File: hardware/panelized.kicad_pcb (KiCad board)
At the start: 2 copper layers, 69.2 x 21 mm, 90 parts, among them J1 USB_B_Micro, J12 Conn_01x01, J2 Conn_01x01, J3 Conn_01x01, J4 Conn_01x01, Q1 Q_DUAL_NPN_NPN_E1B1C2E2B2C1, Q2 Q_PMOS_GSD, Q3 Q_PMOS_GSD, U1 MCP73831-2-OT, U2 CP2104, U3 TPS62400, U4 ESP32-PICO-D4, U5 BD48KxxG

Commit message: To be continued
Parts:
- removed the C1 at (114.8, 106.5)
- removed the C1 at (114.8, 118.5)
- removed C10 (x2), C11 (x2), C13 (x2): 10μF, Capacitor_SMD:C_0402_1005Metric
- removed C12 (x2): 33pF, Capacitor_SMD:C_0402_1005Metric
- removed the C2 at (111.8, 101.1)
- removed the C2 at (111.8, 113.1)
- removed the C5 at (139.0, 103.8)
- removed the C5 at (139.0, 115.8)
- removed the C7 at (138.3, 106.9)
- removed the C7 at (138.3, 118.9)
- removed the D1 at (113.7, 107.7)
- removed the D1 at (113.7, 119.7)
- removed the D2 at (101.1, 102.4)
- removed the D2 at (101.1, 114.4)
- removed the D3 at (112.1, 105.8)
- removed the D3 at (112.1, 117.8)
- removed the JP1 at (137.5, 100.8)
- removed the JP1 at (137.5, 112.8)
- removed L2 (x2), L3 (x2): 2.2μH, Inductor_SMD:L_0805_2012Metric
- removed the Q1 at (137.1, 102.9)
- removed the Q1 at (137.1, 114.9)
- removed the Q3 at (111.8, 103.8)
- removed the Q3 at (111.8, 115.8)
- removed the R10 at (109.0, 101.4)
- removed the R10 at (109.0, 113.4)
- removed the R11 at (108.0, 107.5)
- removed the R11 at (108.0, 119.5)
- removed the R12 at (110.0, 107.5)
- removed the R12 at (110.0, 119.5)
- removed the R14 at (111.7, 106.8)
- removed the R14 at (111.7, 118.8)
- removed the R2 at (114.8, 105.0)
- removed the R2 at (114.8, 117.0)
- removed the R3 at (117.7, 105.9)
- removed the R3 at (117.7, 117.9)
- removed the R4 at (115.7, 107.7)
- removed the R4 at (115.7, 119.7)
- removed R5 (x2): 470kΩ, Resistor_SMD:R_0402_1005Metric
- removed the R6 at (109.2, 105.6)
- removed the R6 at (109.2, 117.6)
- removed the R7 at (126.8, 102.0)
- removed the R7 at (126.8, 114.0)
- removed the R8 at (125.6, 102.0)
- removed the R8 at (125.6, 114.0)
- removed the R9 at (108.0, 101.4)
- removed the R9 at (108.0, 113.4)
- removed the REF** at (98.3, 116.5)
- removed the REF** at (98.3, 104.5)
- removed the U1 at (114.8, 102.0)
- removed the U1 at (114.8, 114.0)
- removed the U3 at (105.7, 104.4)
- removed the U3 at (105.7, 116.4)
- removed the U4 at (131.5, 104.2)
- removed the U4 at (131.5, 116.2)
- removed the U5 at (103.7, 101.7)
- removed the U5 at (103.7, 113.7)
- added C1: 4.7μF, Capacitor_SMD:C_0402_1005Metric, F.Cu at (116.0, 118.1)
- added C1: 4.7μF, Capacitor_SMD:C_0402_1005Metric, F.Cu at (116.0, 106.1)
- added C2: 4.7μF, Capacitor_SMD:C_0402_1005Metric, F.Cu at (111.6, 113.1)
- added C2: 4.7μF, Capacitor_SMD:C_0402_1005Metric, F.Cu at (111.6, 101.1)
- added C3: 4.7μF, Capacitor_SMD:C_0402_1005Metric, F.Cu at (139.0, 115.8)
- added C3: 4.7μF, Capacitor_SMD:C_0402_1005Metric, F.Cu at (139.0, 103.8)
- added C4: 4.7μF, Capacitor_SMD:C_0402_1005Metric, F.Cu at (108.9, 115.6)
- added C4: 4.7μF, Capacitor_SMD:C_0402_1005Metric, F.Cu at (108.9, 103.6)
- added C5: 10μF, Capacitor_SMD:C_0402_1005Metric, F.Cu at (103.1, 114.9)
- added C5: 10μF, Capacitor_SMD:C_0402_1005Metric, F.Cu at (103.1, 102.9)
- added C6: 120pF, Capacitor_SMD:C_0402_1005Metric, F.Cu at (105.0, 119.3)
- added C6: 120pF, Capacitor_SMD:C_0402_1005Metric, F.Cu at (105.0, 107.3)
- added C7: 4.7μF, Capacitor_SMD:C_0402_1005Metric, F.Cu at (108.9, 116.6)
- added C7: 4.7μF, Capacitor_SMD:C_0402_1005Metric, F.Cu at (108.9, 104.6)
- added C8: 1.5pF, Capacitor_SMD:C_0402_1005Metric, F.Cu at (138.3, 118.9)
- added C8: 1.5pF, Capacitor_SMD:C_0402_1005Metric, F.Cu at (138.3, 106.9)
- added C9: 10μF, Capacitor_SMD:C_0402_1005Metric, F.Cu at (101.5, 115.6)
- added C9: 10μF, Capacitor_SMD:C_0402_1005Metric, F.Cu at (101.5, 103.6)
- added D1: LED_Small_ALT, LED_SMD:LED_0402_1005Metric, F.Cu at (114.5, 116.4)
- added D1: LED_Small_ALT, LED_SMD:LED_0402_1005Metric, F.Cu at (114.5, 104.4)
- added D2: D_ALT, Diode_SMD:D_0402_1005Metric, F.Cu at (101.5, 114.4)
- added D2: D_ALT, Diode_SMD:D_0402_1005Metric, F.Cu at (101.5, 102.4)
- added D3: D_Schottky, Diode_SMD:D_0402_1005Metric, F.Cu at (111.7, 117.5)
- added D3: D_Schottky, Diode_SMD:D_0402_1005Metric, F.Cu at (111.7, 105.5)
- added G***: LOGO, double-oh:OSHW_mark, B.Cu at (112.8, 115.3)
- added G***: LOGO, double-oh:OSHW_mark, B.Cu at (112.8, 103.3)
- added JP1: Jumper_NO_Small, double-oh:solder_bridge, F.Cu at (137.1, 113.2)
- added JP1: Jumper_NO_Small, double-oh:solder_bridge, F.Cu at (137.1, 101.2)
- added JP3: Jumper_NO_Small, double-oh:solder_bridge, F.Cu at (129.7, 119.5)
- added JP3: Jumper_NO_Small, double-oh:solder_bridge, F.Cu at (129.7, 107.5)
- added Q1: Q_DUAL_NPN_NPN_E1B1C2E2B2C1, Package_TO_SOT_SMD:SOT-363_SC-70-6, F.Cu at (137.1, 115.3)
- added Q1: Q_DUAL_NPN_NPN_E1B1C2E2B2C1, Package_TO_SOT_SMD:SOT-363_SC-70-6, F.Cu at (137.1, 103.3)
- added Q3: Q_PMOS_GSD, Package_TO_SOT_SMD:SOT-323_SC-70, F.Cu at (111.3, 115.3)
- added Q3: Q_PMOS_GSD, Package_TO_SOT_SMD:SOT-323_SC-70, F.Cu at (111.3, 103.3)
- added R10: 68kΩ, Resistor_SMD:R_0402_1005Metric, F.Cu at (104.8, 117.4)
- added R10: 68kΩ, Resistor_SMD:R_0402_1005Metric, F.Cu at (104.8, 105.4)
- added R11: 68kΩ, Resistor_SMD:R_0402_1005Metric, F.Cu at (109.2, 119.5)
- added R11: 68kΩ, Resistor_SMD:R_0402_1005Metric, F.Cu at (109.2, 107.5)
- added R12: 300kΩ, Resistor_SMD:R_0402_1005Metric, F.Cu at (110.2, 119.5)
- added R12: 300kΩ, Resistor_SMD:R_0402_1005Metric, F.Cu at (110.2, 107.5)
- added R14: 68kΩ, Resistor_SMD:R_0402_1005Metric, F.Cu at (111.7, 118.5)
- added R14: 68kΩ, Resistor_SMD:R_0402_1005Metric, F.Cu at (111.7, 106.5)
- added R2: 3kΩ, Resistor_SMD:R_0402_1005Metric, F.Cu at (117.1, 113.8)
- added R2: 3kΩ, Resistor_SMD:R_0402_1005Metric, F.Cu at (117.1, 101.8)
- added R3: 68kΩ, Resistor_SMD:R_0402_1005Metric, F.Cu at (117.7, 118.5)
- added R3: 68kΩ, Resistor_SMD:R_0402_1005Metric, F.Cu at (117.7, 106.5)
- added R4: 2kΩ, Resistor_SMD:R_0402_1005Metric, F.Cu at (116.5, 116.4)
- added R4: 2kΩ, Resistor_SMD:R_0402_1005Metric, F.Cu at (116.5, 104.4)
- added R6: 68kΩ, Resistor_SMD:R_0402_1005Metric, F.Cu at (104.4, 113.6)
- added R6: 68kΩ, Resistor_SMD:R_0402_1005Metric, F.Cu at (104.4, 101.6)
- added R7: 68kΩ, Resistor_SMD:R_0402_1005Metric, F.Cu at (126.2, 114.2)
- added R7: 68kΩ, Resistor_SMD:R_0402_1005Metric, F.Cu at (126.2, 102.2)
- added R8: 1kΩ, Resistor_SMD:R_0402_1005Metric, F.Cu at (126.2, 116.2)
- added R8: 1kΩ, Resistor_SMD:R_0402_1005Metric, F.Cu at (126.2, 104.2)
- added R9: 330kΩ, Resistor_SMD:R_0402_1005Metric, F.Cu at (103.9, 119.3)
- added R9: 330kΩ, Resistor_SMD:R_0402_1005Metric, F.Cu at (103.9, 107.3)
- added REF**: mousebite_mount, double-oh:mousebite_mount, F.Cu at (98.4, 104.5)
- added REF**: mousebite_mount, double-oh:mousebite_mount, F.Cu at (98.4, 116.5)
- added REF**: Fiducial_0.5mm_Mask1.5mm, Fiducial:Fiducial_0.5mm_Mask1.5mm, F.Cu at (146.5, 115.6)
- added REF**: Fiducial_0.5mm_Mask1.5mm, Fiducial:Fiducial_0.5mm_Mask1.5mm, F.Cu at (99.5, 117.3)
- added REF**: Fiducial_0.5mm_Mask1.5mm, Fiducial:Fiducial_0.5mm_Mask1.5mm, F.Cu at (99.5, 105.3)
- added REF**: Fiducial_0.5mm_Mask1.5mm, Fiducial:Fiducial_0.5mm_Mask1.5mm, F.Cu at (146.5, 103.6)
- added U1: MCP73831-2-OT, Package_TO_SOT_SMD:SOT-23-5, F.Cu at (114.7, 114.0)
- added U1: MCP73831-2-OT, Package_TO_SOT_SMD:SOT-23-5, F.Cu at (114.7, 102.0)
- added U3: TPSM828x, double-oh:microSiL-10, F.Cu at (105.2, 115.5)
- added U3: TPSM828x, double-oh:microSiL-10, F.Cu at (105.2, 103.5)
- added U4: ESP32-U4WDH, Package_DFN_QFN:QFN-48-1EP_5x5mm_P0.35mm_EP3.7x3.7mm, F.Cu at (131.6, 115.7)
- added U4: ESP32-U4WDH, Package_DFN_QFN:QFN-48-1EP_5x5mm_P0.35mm_EP3.7x3.7mm, F.Cu at (131.6, 103.7)
- added U5: XC6120CxxxHR, double-oh:USP-3, F.Cu at (109.0, 114.0)
- added U5: XC6120CxxxHR, double-oh:USP-3, F.Cu at (109.0, 102.0)
- added U6: TPSM828x, double-oh:microSiL-10, F.Cu at (107.1, 119.3)
- added U6: TPSM828x, double-oh:microSiL-10, F.Cu at (107.1, 107.3)
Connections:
- AE1 pad 1: (no net) -> Net-(AE1-Pad1) (x2)
- J1 pad 1: (no net) -> USB_VIN (x2)
- J1 pad 2: (no net) -> Net-(J1-Pad2) (x2)
- J1 pad 3: (no net) -> Net-(J1-Pad3) (x2)
- J1 pad 5: (no net) -> 0V (x2)
- J2 pad 1: (no net) -> to_top_cap (x2)
- J3 pad 1: (no net) -> LIPO_V (x2)
- J4 pad 1: (no net) -> 0V (x2)
- L1 pad 1: (no net) -> Net-(AE1-Pad1) (x2)
- L1 pad 2: (no net) -> Net-(C8-Pad2) (x2)
- Q2 pad 1: (no net) -> Net-(Q2-Pad1) (x2)
- Q2 pad 2: (no net) -> batt_out (x2)
- Q2 pad 3: (no net) -> to_top_cap (x2)
- R1 pad 1: (no net) -> LIPO_V (x2)
- R1 pad 2: (no net) -> ADC (x2)
- R13 pad 1: (no net) -> 3.3V (x2)
- R13 pad 2: (no net) -> EN (x2)
- U2 pad 19: (no net) -> RTS (x2)
- U2 pad 2: (no net) -> 0V (x2)
- U2 pad 20: (no net) -> RX_USB (x2)
- U2 pad 21: (no net) -> RX_ESP (x2)
- U2 pad 23: (no net) -> DTR (x2)
- U2 pad 25: (no net) -> 0V (x2)
- U2 pad 3: (no net) -> Net-(J1-Pad3) (x2)
- U2 pad 4: (no net) -> Net-(J1-Pad2) (x2)
- U2 pad 5: (no net) -> Net-(U2-Pad5) (x2)
- U2 pad 6: (no net) -> Net-(U2-Pad5) (x2)
- U2 pad 7: (no net) -> USB_VIN (x2)
- U2 pad 8: (no net) -> USB_VIN (x2)
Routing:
- net (no net): track 915.2 -> 0.00 mm, vias 92 -> 0
- net 3.3V: track 0.00 -> 120.8 mm, vias 0 -> 8
- net 0V: track 0.00 -> 111.8 mm, vias 0 -> 56
- net Net-(R12-Pad2): track 0.00 -> 62.7 mm, vias 0 -> 4
- net Net-(Q2-Pad1): track 0.00 -> 55.6 mm, vias 0 -> 4
- net LIPO_V: track 0.00 -> 49.6 mm, vias 0 -> 2
- net USB_VIN: track 0.00 -> 49.0 mm, vias 0 -> 4
- net ADC: track 0.00 -> 47.2 mm, vias 0 -> 4
- net DTR: track 0.00 -> 43.0 mm
- net RTS: track 0.00 -> 39.3 mm, vias 0 -> 4
- net TPS_VIN: track 0.00 -> 27.8 mm, vias 0 -> 4
- net Net-(C8-Pad2): track 0.00 -> 23.7 mm
- net EN: track 0.00 -> 21.3 mm
- net TPS_EN: track 0.00 -> 17.9 mm, vias 0 -> 4
- net RX_USB: track 0.00 -> 17.7 mm
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- added copper zone on B.Cu, net 0V
- added copper zone on F.Cu, net 0V
- added copper zone on F.Cu, net 3.3V
- added copper zone on F.Cu, net TPS_VIN
- added copper zone on F.Cu, net batt_out
- removed copper zone on B.Cu, net (none)
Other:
- net class Default: trace_width 0.25 -> 0.2
- net class Larger added: clearance 0.2, trace_width 0.4, via_dia 0.8, via_drill 0.4
- net class U4WDH added: clearance 0.14, trace_width 0.2, via_dia 0.8, via_drill 0.4
- rule pad_to_mask_clearance: 0.051 -> 0
- board text added: "Double-Oh v3.0 // July 2021"
- board text removed: "Double-Oh v2.7 // Sept. 2020"

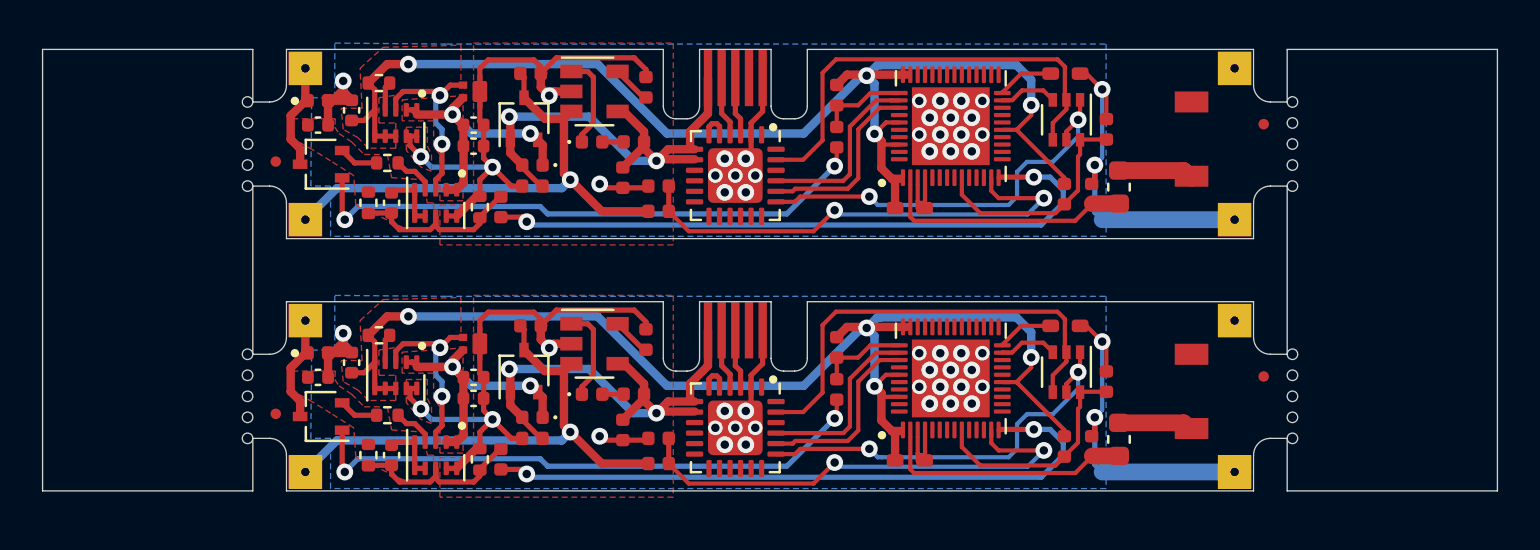
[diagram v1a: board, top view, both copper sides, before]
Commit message: Update resistor values
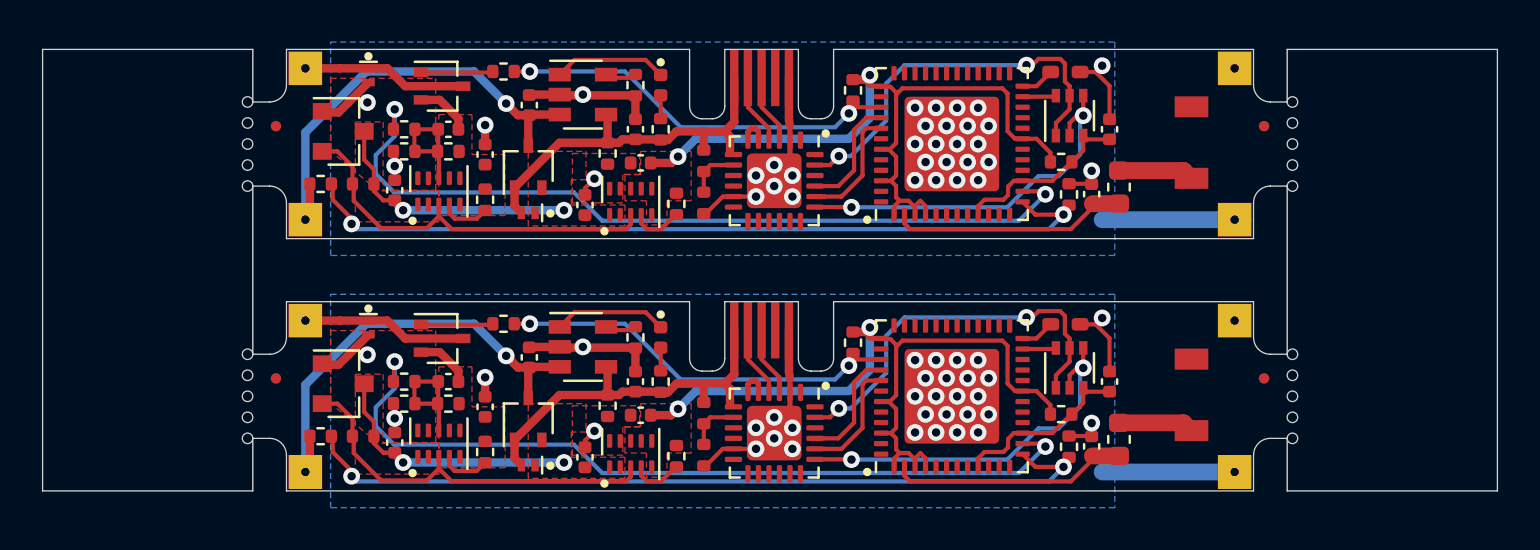
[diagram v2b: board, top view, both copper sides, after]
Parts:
- removed the C1 at (116.0, 118.1)
- removed the C1 at (116.0, 106.1)
- removed the C2 at (111.6, 113.1)
- removed the C2 at (111.6, 101.1)
- removed the C3 at (139.0, 115.8)
- removed the C3 at (139.0, 103.8)
- removed the C4 at (108.9, 115.6)
- removed the C4 at (108.9, 103.6)
- removed the C5 at (103.1, 114.9)
- removed the C5 at (103.1, 102.9)
- removed the C6 at (105.0, 119.3)
- removed the C6 at (105.0, 107.3)
- removed the C7 at (108.9, 116.6)
- removed the C7 at (108.9, 104.6)
- removed the C9 at (101.5, 115.6)
- removed the C9 at (101.5, 103.6)
- removed the D1 at (114.5, 116.4)
- removed the D1 at (114.5, 104.4)
- removed the D2 at (101.5, 114.4)
- removed the D2 at (101.5, 102.4)
- removed the D3 at (111.7, 117.5)
- removed the D3 at (111.7, 105.5)
- removed the J1 at (121.3, 113.3)
- removed the J1 at (121.3, 101.3)
- removed the JP1 at (137.1, 113.2)
- removed the JP1 at (137.1, 101.2)
- removed JP3 (x2): Jumper_NO_Small, double-oh:solder_bridge
- removed the Q1 at (137.1, 115.3)
- removed the Q1 at (137.1, 103.3)
- removed the Q2 at (101.7, 117.5)
- removed the Q2 at (101.7, 105.5)
- removed the Q3 at (111.3, 115.3)
- removed the Q3 at (111.3, 103.3)
- removed the R1 at (117.7, 119.7)
- removed the R1 at (117.7, 107.7)
- removed the R10 at (104.8, 117.4)
- removed the R10 at (104.8, 105.4)
- removed the R11 at (109.2, 119.5)
- removed the R11 at (109.2, 107.5)
- removed the R12 at (110.2, 119.5)
- removed the R12 at (110.2, 107.5)
- removed the R13 at (137.0, 118.9)
- removed the R13 at (137.0, 106.9)
- removed the R14 at (111.7, 118.5)
- removed the R14 at (111.7, 106.5)
- removed the R2 at (117.1, 113.8)
- removed the R2 at (117.1, 101.8)
- removed the R3 at (117.7, 118.5)
- removed the R3 at (117.7, 106.5)
- removed the R4 at (116.5, 116.4)
- removed the R4 at (116.5, 104.4)
- removed the R6 at (104.4, 113.6)
- removed the R6 at (104.4, 101.6)
- removed the R7 at (126.2, 114.2)
- removed the R7 at (126.2, 102.2)
- removed the R8 at (126.2, 116.2)
- removed the R8 at (126.2, 104.2)
- removed the R9 at (103.9, 119.3)
- removed the R9 at (103.9, 107.3)
- removed the REF** at (147.6, 116.5)
- removed the REF** at (147.6, 104.5)
- removed the REF** at (98.4, 104.5)
- removed the REF** at (98.4, 116.5)
- removed the REF** at (146.5, 115.6)
- removed the REF** at (99.5, 117.3)
- removed the REF** at (99.5, 105.3)
- removed the REF** at (146.5, 103.6)
- removed the U1 at (114.7, 114.0)
- removed the U1 at (114.7, 102.0)
- removed the U2 at (121.3, 118.0)
- removed the U2 at (121.3, 106.0)
- removed the U3 at (105.2, 115.5)
- removed the U3 at (105.2, 103.5)
- removed the U4 at (131.6, 115.7)
- removed the U4 at (131.6, 103.7)
- removed the U5 at (109.0, 114.0)
- removed the U5 at (109.0, 102.0)
- removed the U6 at (107.1, 119.3)
- removed the U6 at (107.1, 107.3)
- added C1: 4.7μF, Capacitor_SMD:C_0402_1005Metric, F.Cu at (116.6, 115.8)
- added C1: 4.7μF, Capacitor_SMD:C_0402_1005Metric, F.Cu at (116.6, 103.8)
- added C2: 4.7μF, Capacitor_SMD:C_0402_1005Metric, F.Cu at (111.5, 114.7)
- added C2: 4.7μF, Capacitor_SMD:C_0402_1005Metric, F.Cu at (111.5, 102.7)
- added C3: 4.7μF, Capacitor_SMD:C_0402_1005Metric, F.Cu at (139.2, 115.8)
- added C3: 4.7μF, Capacitor_SMD:C_0402_1005Metric, F.Cu at (139.2, 103.8)
- added C4: 4.7μF, Capacitor_SMD:C_0402_1005Metric, F.Cu at (114.2, 119.4)
- added C4: 4.7μF, Capacitor_SMD:C_0402_1005Metric, F.Cu at (114.2, 107.4)
- added C5: 10μF, Capacitor_SMD:C_0402_1005Metric, F.Cu at (116.8, 117.4)
- added C5: 10μF, Capacitor_SMD:C_0402_1005Metric, F.Cu at (116.8, 105.4)
- added C6: 120pF, Capacitor_SMD:C_0402_1005Metric, F.Cu at (107.7, 115.8)
- added C6: 120pF, Capacitor_SMD:C_0402_1005Metric, F.Cu at (107.7, 103.8)
- added C7: 4.7μF, Capacitor_SMD:C_0402_1005Metric, F.Cu at (105.2, 118.7)
- added C7: 4.7μF, Capacitor_SMD:C_0402_1005Metric, F.Cu at (105.2, 106.7)
- added C9: 10μF, Capacitor_SMD:C_0402_1005Metric, F.Cu at (109.5, 117.0)
- added C9: 10μF, Capacitor_SMD:C_0402_1005Metric, F.Cu at (109.5, 105.0)
- added D1: Blue LED, LED_SMD:LED_0402_1005Metric, F.Cu at (117.8, 113.7)
- added D1: Blue LED, LED_SMD:LED_0402_1005Metric, F.Cu at (117.8, 101.7)
- added D2: ‎PMEG6010AESBYL‎, double-oh:SOD-993, F.Cu at (103.9, 113.2)
- added D2: ‎PMEG6010AESBYL‎, double-oh:SOD-993, F.Cu at (103.9, 101.2)
- added D3: ‎PMEG6010AESBYL‎, double-oh:SOD-993, F.Cu at (111.5, 119.8)
- added D3: ‎PMEG6010AESBYL‎, double-oh:SOD-993, F.Cu at (111.5, 107.8)
- added J1: Unshielded USB Micro port, double-oh:microusb_PCB_socket, F.Cu at (122.6, 113.3)
- added J1: Unshielded USB Micro port, double-oh:microusb_PCB_socket, F.Cu at (122.6, 101.3)
- added JP1: Jumper_NO_Small, double-oh:solder_bridge, F.Cu at (137.1, 113.1)
- added JP1: Jumper_NO_Small, double-oh:solder_bridge, F.Cu at (137.1, 101.1)
- added Q1: MUN5213DW1, Package_TO_SOT_SMD:SOT-363_SC-70-6, F.Cu at (137.2, 115.2)
- added Q1: MUN5213DW1, Package_TO_SOT_SMD:SOT-363_SC-70-6, F.Cu at (137.2, 103.2)
- added Q2: Q_PMOS_GSD, Package_TO_SOT_SMD:SOT-323_SC-70, F.Cu at (107.4, 113.8)
- added Q2: Q_PMOS_GSD, Package_TO_SOT_SMD:SOT-323_SC-70, F.Cu at (107.4, 101.8)
- added Q3: Q_PMOS_GSD, Package_TO_SOT_SMD:SOT-323_SC-70, F.Cu at (111.5, 117.6)
- added Q3: Q_PMOS_GSD, Package_TO_SOT_SMD:SOT-323_SC-70, F.Cu at (111.5, 105.6)
- added R1: 68kΩ, Resistor_SMD:R_0402_1005Metric, F.Cu at (101.6, 118.4)
- added R1: 68kΩ, Resistor_SMD:R_0402_1005Metric, F.Cu at (101.6, 106.4)
- added R10: 68kΩ, Resistor_SMD:R_0402_1005Metric, F.Cu at (109.5, 119.2)
- added R10: 68kΩ, Resistor_SMD:R_0402_1005Metric, F.Cu at (109.5, 107.2)
- added R11: 68kΩ, Resistor_SMD:R_0402_1005Metric, F.Cu at (105.6, 116.8)
- added R11: 68kΩ, Resistor_SMD:R_0402_1005Metric, F.Cu at (105.6, 104.8)
- added R12: 300kΩ, Resistor_SMD:R_0402_1005Metric, F.Cu at (105.6, 115.8)
- added R12: 300kΩ, Resistor_SMD:R_0402_1005Metric, F.Cu at (105.6, 103.8)
- added R13: 68kΩ, Resistor_SMD:R_0402_1005Metric, F.Cu at (136.8, 117.3)
- added R13: 68kΩ, Resistor_SMD:R_0402_1005Metric, F.Cu at (136.8, 105.3)
- added R14: 24kΩ, Resistor_SMD:R_0402_1005Metric, F.Cu at (119.8, 117.3)
- added R14: 24kΩ, Resistor_SMD:R_0402_1005Metric, F.Cu at (119.8, 105.3)
- added R15: 47kΩ, Resistor_SMD:R_0402_1005Metric, F.Cu at (119.8, 119.3)
- added R15: 47kΩ, Resistor_SMD:R_0402_1005Metric, F.Cu at (119.8, 107.3)
- added R16: 68kΩ, Resistor_SMD:R_0402_1005Metric, F.Cu at (103.7, 118.4)
- added R16: 68kΩ, Resistor_SMD:R_0402_1005Metric, F.Cu at (103.7, 106.4)
- added R2: 3kΩ, Resistor_SMD:R_0402_1005Metric, F.Cu at (116.6, 113.7)
- added R2: 3kΩ, Resistor_SMD:R_0402_1005Metric, F.Cu at (116.6, 101.7)
- added R3: 68kΩ, Resistor_SMD:R_0402_1005Metric, F.Cu at (137.2, 118.9)
- added R3: 68kΩ, Resistor_SMD:R_0402_1005Metric, F.Cu at (137.2, 106.9)
- added R4: 2kΩ, Resistor_SMD:R_0402_1005Metric, F.Cu at (117.8, 115.8)
- added R4: 2kΩ, Resistor_SMD:R_0402_1005Metric, F.Cu at (117.8, 103.8)
- added R5: 68kΩ, Resistor_SMD:R_0402_1005Metric, F.Cu at (115.3, 117.0)
- added R5: 68kΩ, Resistor_SMD:R_0402_1005Metric, F.Cu at (115.3, 105.0)
- added R6: 68kΩ, Resistor_SMD:R_0402_1005Metric, F.Cu at (118.5, 119.3)
- added R6: 68kΩ, Resistor_SMD:R_0402_1005Metric, F.Cu at (118.5, 107.3)
- added R7: 68kΩ, Resistor_SMD:R_0402_1005Metric, F.Cu at (127.0, 114.0)
- added R7: 68kΩ, Resistor_SMD:R_0402_1005Metric, F.Cu at (127.0, 102.0)
- added R8: 1kΩ, Resistor_SMD:R_0402_1005Metric, F.Cu at (110.3, 113.0)
- added R8: 1kΩ, Resistor_SMD:R_0402_1005Metric, F.Cu at (110.3, 101.0)
- added R9: 330kΩ, Resistor_SMD:R_0402_1005Metric, F.Cu at (107.7, 116.8)
- added R9: 330kΩ, Resistor_SMD:R_0402_1005Metric, F.Cu at (107.7, 104.8)
- added REF**: mousebite_mount_4, double-oh:mousebite_mount_4, F.Cu at (98.4, 118.5)
- added REF**: Fiducial_0.5mm_Mask1.5mm, Fiducial:Fiducial_0.5mm_Mask1.5mm, F.Cu at (99.5, 115.7)
- added REF**: Fiducial_0.5mm_Mask1.5mm, Fiducial:Fiducial_0.5mm_Mask1.5mm, F.Cu at (146.5, 115.7)
- added REF**: Fiducial_0.5mm_Mask1.5mm, Fiducial:Fiducial_0.5mm_Mask1.5mm, F.Cu at (99.5, 103.7)
- added REF**: Fiducial_0.5mm_Mask1.5mm, Fiducial:Fiducial_0.5mm_Mask1.5mm, F.Cu at (146.5, 103.7)
- added U1: ESP32-PICO-V3, double-oh:QFN-48-1EP_7x7mm_P0.5mm_EP4.5x4.5mm, F.Cu at (131.7, 116.5)
- added U1: ESP32-PICO-V3, double-oh:QFN-48-1EP_7x7mm_P0.5mm_EP4.5x4.5mm, F.Cu at (131.7, 104.5)
- added U2: CP2102N, Package_DFN_QFN:QFN-24-1EP_4x4mm_P0.5mm_EP2.6x2.6mm, F.Cu at (123.2, 118.2)
- added U2: CP2102N, Package_DFN_QFN:QFN-24-1EP_4x4mm_P0.5mm_EP2.6x2.6mm, F.Cu at (123.2, 106.2)
- added U3: TPSM828214SILR, double-oh:microSiL-10, F.Cu at (116.4, 119.2)
- added U3: TPSM828214SILR, double-oh:microSiL-10, F.Cu at (116.4, 107.2)
- added U4: TPSM82821SILR, double-oh:microSiL-10, F.Cu at (107.2, 118.8)
- added U4: TPSM82821SILR, double-oh:microSiL-10, F.Cu at (107.2, 106.8)
- added U5: MCP73831-2-OT, Package_TO_SOT_SMD:SOT-23-5, F.Cu at (114.1, 114.2)
- added U5: MCP73831-2-OT, Package_TO_SOT_SMD:SOT-23-5, F.Cu at (114.1, 102.2)
- added U6: BD48KxxG, Package_TO_SOT_SMD:SOT-23, F.Cu at (102.7, 115.9)
- added U6: BD48KxxG, Package_TO_SOT_SMD:SOT-23, F.Cu at (102.7, 103.9)
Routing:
- net 0V: track 111.8 -> 61.8 mm, vias 56 -> 66
- net Net-(Q2-Pad1): track 55.6 -> 7.34 mm, vias 4 -> 0
- net 3.3V: track 120.8 -> 73.1 mm, vias 8 -> 4
- net ADC: track 47.2 -> 78.7 mm
- net Net-(R7-Pad2): track 8.49 -> 38.5 mm, vias 0 -> 4
- net TPS_EN: track 17.9 -> 37.6 mm, vias 4 -> 0
- net Net-(R12-Pad2): track 62.7 -> 77.7 mm
- net USB_VIN: track 49.0 -> 37.5 mm, vias 4 -> 0
- net /D-: track 0.00 -> 6.75 mm
- net /D+: track 0.00 -> 6.63 mm
- net RX_USB: track 17.7 -> 11.4 mm
- net RX_ESP: track 17.6 -> 11.2 mm
- net DAC: track 17.5 -> 11.3 mm
- net Net-(JP3-Pad1): track 5.78 -> 0.00 mm
- net Net-(J1-Pad2): track 5.76 -> 0.00 mm
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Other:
- outline, holes or cut-outs redrawn
